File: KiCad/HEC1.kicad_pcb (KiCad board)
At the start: 2 copper layers, 243.8 x 170.2 mm, 618 parts, among them J1 Barrel_Jack_Switch, J2 Conn_02x12_Odd_Even, J3 Conn_02x05_Odd_Even, J5 Screw_Terminal_01x02, J6 DE9_Plug_MountingHoles, J7 AudioJack3, J8 NES_Port_Male, J9 Conn_02x14_Odd_Even, SW1 SW_DIP_x04, SW2 SW_Push, U1 Z80CPU, U10 74LS32, U11 74LS00, U12 74LS04, U13 74LS245, U14 74LS245, U15 74LS32, U16 74LS32, U17 74LS20, U18 74LS138, U19 74LS30, U2 AS6C4008-55PCN, U20 74LS574, U21 74LS574, U22 74LS02, U23 74LS74, U24 74LS74, U25 74LS541, U26 74LS541, U27 74LS74, U28 74LS30, U29 74LS74, U3 AS6C4008-55PCN, U30 74LS74, U31 74LS32, U32 LM79M05_TO220, U33 74LS20, U34 74LS393, U35 74LS08, U36 74LS574, U37 74LS32, U38 74LS47, U39 74LS47, U4 CY7C199, U40 DA04-11EWA, U41 74LS02, U42 74LS06, U44 74LS541, U5 CY7C199, U6 74LS138, U7 28C256, U8 74LS138, U9 74LS574, X1 CXO_DIP8, Y1 Crystal

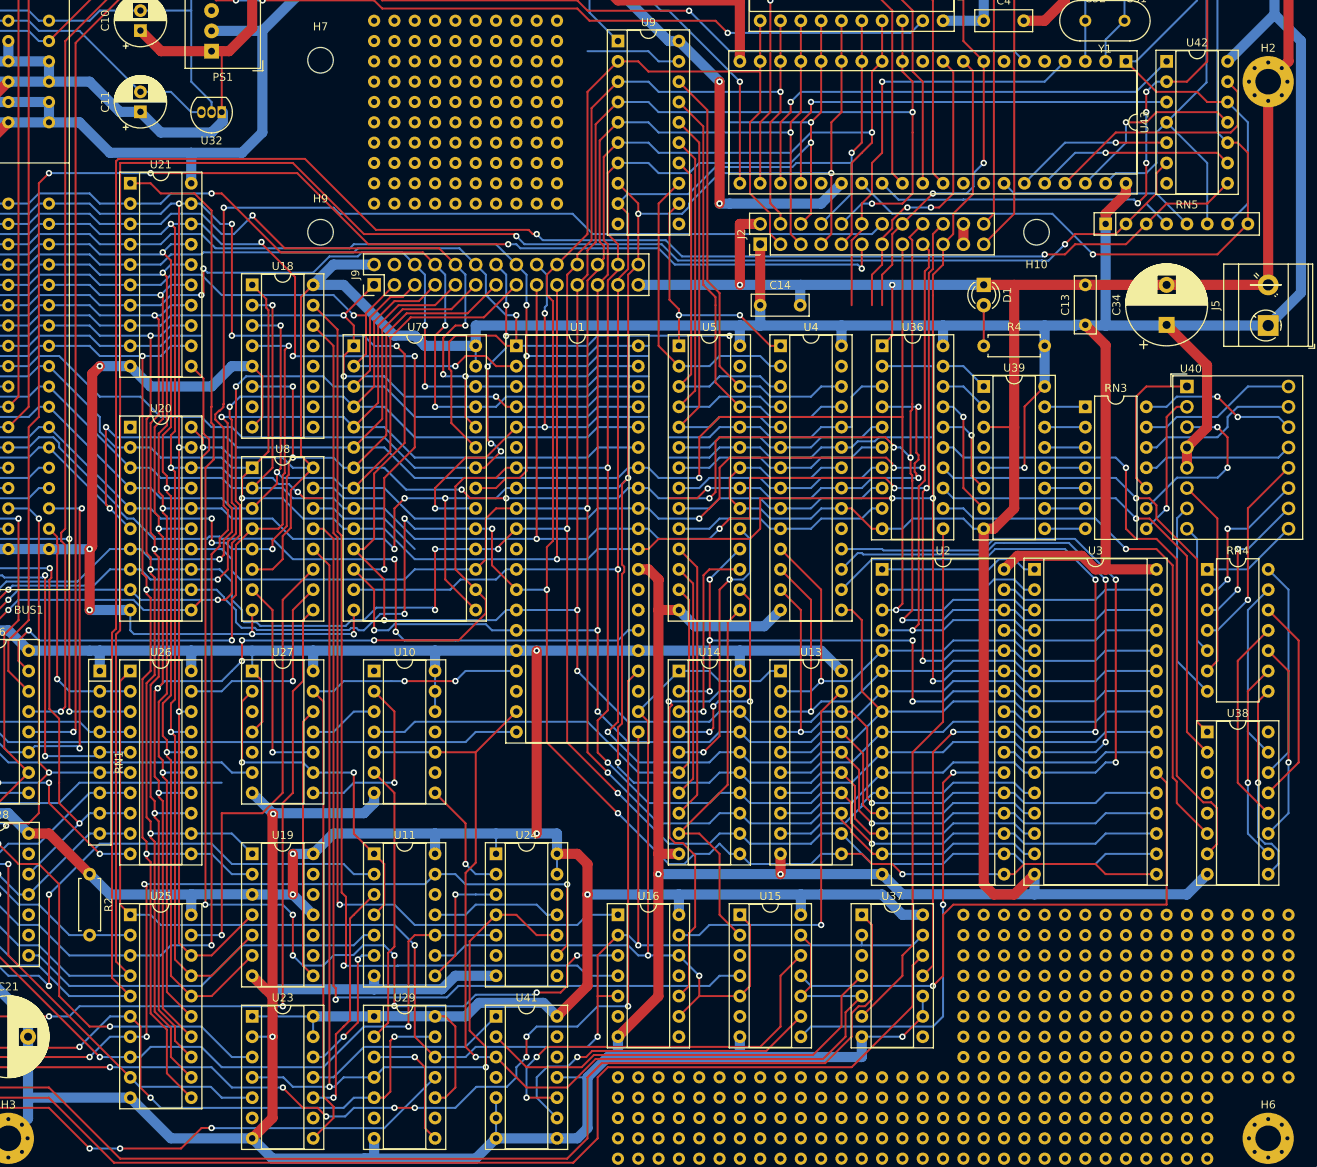
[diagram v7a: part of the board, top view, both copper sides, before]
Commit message: Finish routing data bus
finished routing arguably the hardest part of the board: the data bus. The routing is mostly complete. However, the rest of traces are very hard to route. One more day of work is expected.
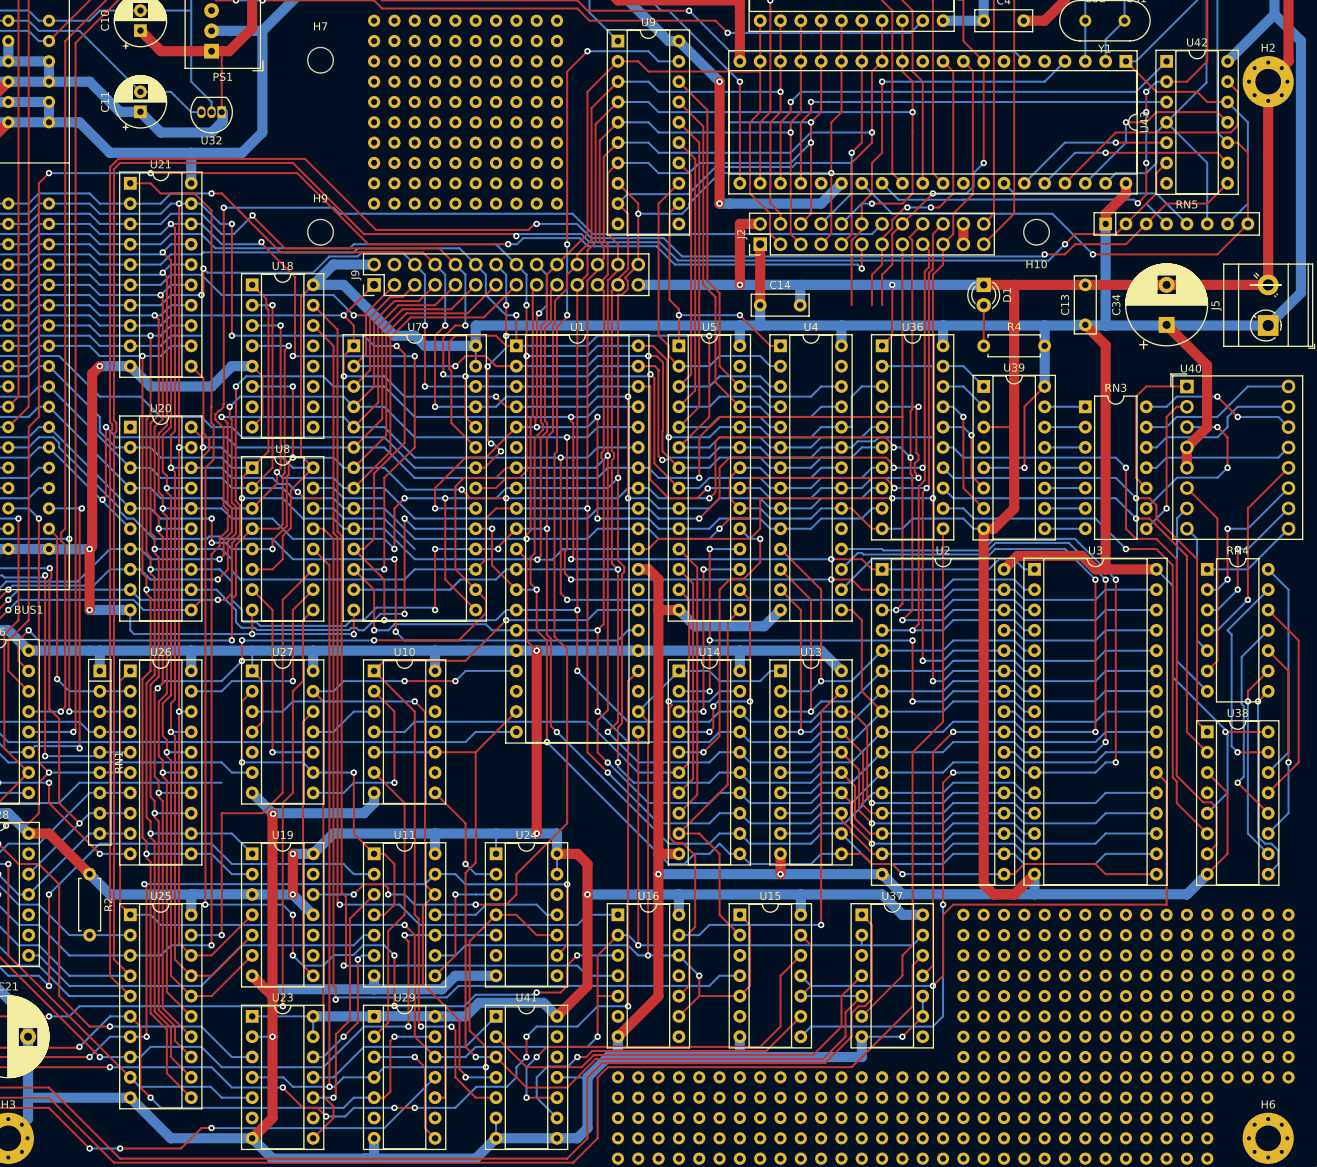
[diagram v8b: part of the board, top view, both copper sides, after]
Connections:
- U41 pad 12: /HEC_Protection/~{M1} -> L
- U41 pad 13: /HEC_Protection/M1 -> unconnected-(U41-Pad13)
- U41 pad 4: unconnected-(U41-Pad4) -> /HEC_Protection/M1
- U41 pad 5: L -> /HEC_Protection/~{M1}
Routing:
- net /HEC_Memory/SYSGATE: track 12.0 -> 150.3 mm, vias 0 -> 6
- net /HEC_Protection/~{M1}: track 0.00 -> 99.5 mm, vias 0 -> 3
- net /HEC_Protection/M1: track 0.00 -> 75.5 mm, vias 0 -> 2
- net /HEC_IO/A5: track 159.0 -> 232.2 mm, vias 3 -> 5
- net /HEC_IO/A7: track 159.7 -> 217.4 mm, vias 3 -> 6
- net /HEC_IO/A6: track 158.4 -> 216.1 mm, vias 3 -> 6
- net H: track 1613.7 -> 1661.9 mm, vias 9 -> 10
- net /HEC_IO/A15: track 176.3 -> 193.9 mm, vias 3 -> 5
- net /HEC_IO/A14: track 189.4 -> 206.4 mm, vias 3 -> 5
- net /HEC_IO/A8: track 215.4 -> 231.8 mm
- net /HEC_IO/A12: track 190.7 -> 206.9 mm, vias 2 -> 3
- net /HEC_IO/A13: track 193.3 -> 209.3 mm, vias 4 -> 5
- net /HEC_IO/A9: track 224.6 -> 239.8 mm, vias 4 -> 5
- net /HEC_IO/A11: track 216.8 -> 229.8 mm
- net /HEC_IO/A10: track 213.1 -> 225.9 mm, vias 2 -> 3
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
